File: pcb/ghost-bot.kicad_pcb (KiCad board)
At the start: 2 copper layers, 111 x 60 mm, 35 parts, among them J1 Conn_01x03_Pin, J2 Conn_01x03_Pin, J3 Conn_01x04_Pin, J4 Conn_01x02_Pin, SW1 SW_Push, SW2 SW_Push, SW3 Switch

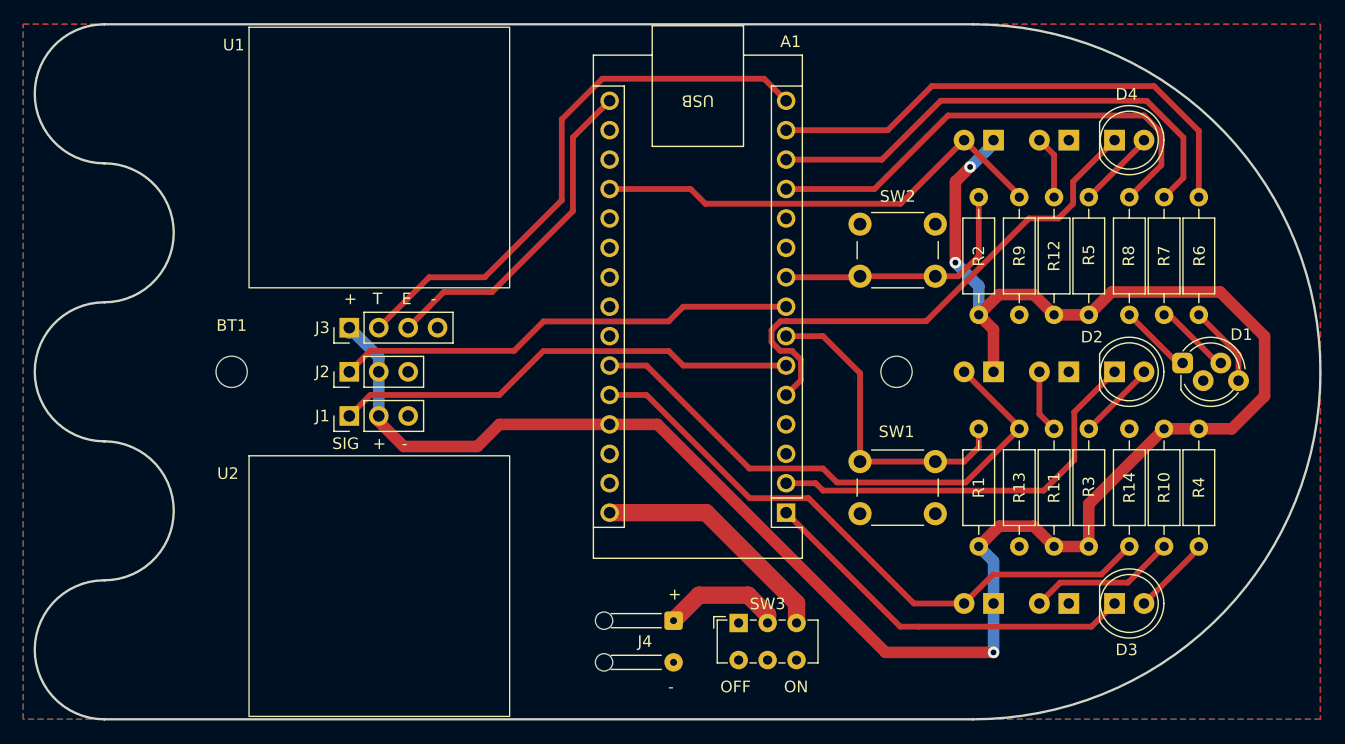
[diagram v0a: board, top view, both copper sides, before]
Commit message: Issue-6: Move LEDs, breakout unused pins
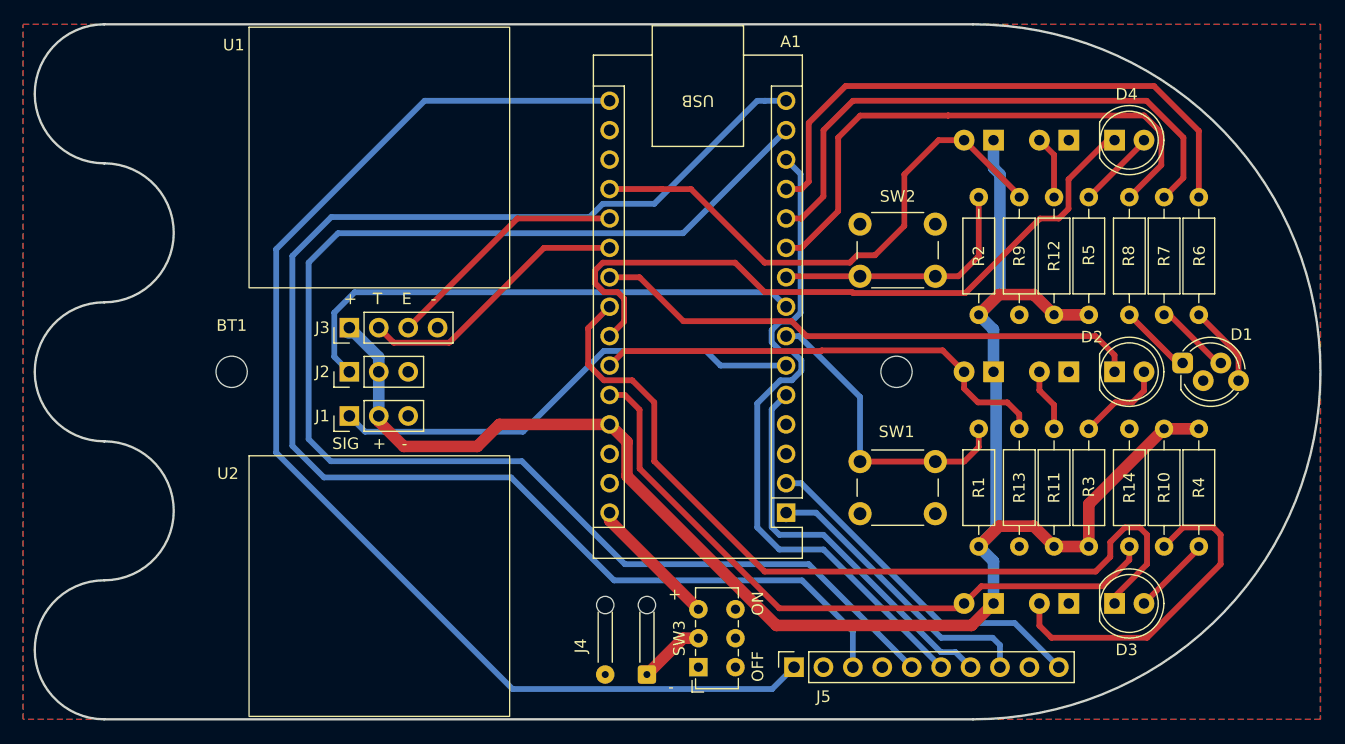
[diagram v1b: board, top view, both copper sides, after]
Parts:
- added J5: Conn_01x10, Connector_PinSocket_2.54mm:PinSocket_1x10_P2.54mm_Vertical, F.Cu at (167.1, 139.5)
- moved J4 5.19 mm to (154.4, 140.1), turned to 180 degrees
- moved SW3 5.16 mm to (158.8, 139.5), turned to 90 degrees
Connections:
- A1 pad 1: /LED1 -> /UART_TX
- A1 pad 10: unconnected-(A1-D7-Pad10) -> /RGB_B
- A1 pad 11: unconnected-(A1-D8-Pad11) -> /RGB_G
- A1 pad 12: /RGB_B -> /RGB_R
- A1 pad 13: /RGB_G -> /SPI_CC
- A1 pad 14: /RGB_R -> /SPI_MOSI
- A1 pad 15: /TRIG -> /SPI_MISO
- A1 pad 16: /ECHO -> /SPI_CLK
- A1 pad 2: /LED0 -> /UART_RX
- A1 pad 20: unconnected-(A1-A1-Pad20) -> /ECHO
- A1 pad 21: unconnected-(A1-A2-Pad21) -> /TRIG
- A1 pad 22: unconnected-(A1-A3-Pad22) -> /LED0
- A1 pad 23: unconnected-(A1-A4-Pad23) -> /LED1
- A1 pad 24: unconnected-(A1-A5-Pad24) -> /LED2
- A1 pad 5: /LED2 -> /GPIO_D2
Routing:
- net /SPI_MISO: track 0.00 -> 122.7 mm
- net /SPI_MOSI: track 0.00 -> 121.4 mm
- net /SPI_CLK: track 0.00 -> 105.6 mm
- net /SPI_CC: track 0.00 -> 58.6 mm
- net /LED1: track 33.3 -> 74.4 mm
- net /GPIO_D2: track 0.00 -> 34.5 mm
- net /UART_RX: track 0.00 -> 30.1 mm
- net /UART_TX: track 0.00 -> 25.7 mm
- net /TRIG: track 49.0 -> 23.9 mm
- net +5V: track 171.7 -> 154.3 mm, vias 3 -> 0
- net Net-(D6-A): track 12.8 -> 29.0 mm
- net /LED2: track 45.3 -> 61.1 mm
- net /LED0: track 35.3 -> 47.8 mm
- net +BATT_SW: track 21.1 -> 11.5 mm
- net /ECHO: track 29.2 -> 21.3 mm
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
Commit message: Separate UART and SPI connectors, reroute tracks, move buttons
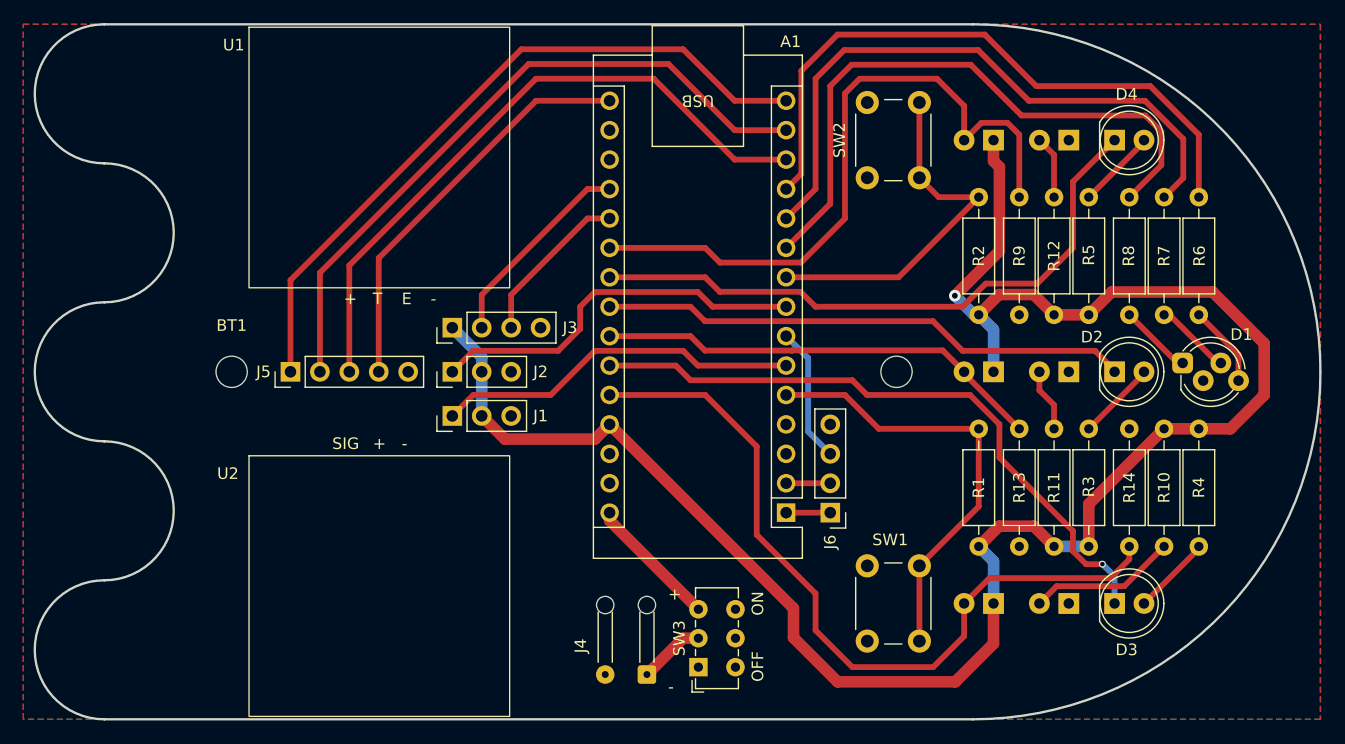
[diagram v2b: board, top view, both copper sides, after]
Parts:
- added J6: Conn_01x04_Pin, Connector_PinHeader_2.54mm:PinHeader_1x04_P2.54mm_Vertical, F.Cu at (170.2, 126.2)
- J5: value Conn_01x10 -> Conn_01x05_Pin; footprint Connector_PinSocket_2.54mm:PinSocket_1x10_P2.54mm_Vertical -> Connector_PinHeader_2.54mm:PinHeader_1x05_P2.54mm_Vertical
- moved J5 50.4 mm to (123.6, 114.0)
- moved SW1 12.5 mm to (173.4, 137.2), turned to 90 degrees
- moved J1 8.89 mm to (137.6, 117.8)
- moved J2 8.89 mm to (137.6, 114.0)
- moved J3 8.89 mm to (137.6, 110.2)
- moved SW2 4.05 mm to (173.4, 97.2), turned to 90 degrees
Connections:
- A1 pad 1: /UART_TX -> /UART_RX
- A1 pad 13: /SPI_CC -> /SPI_MISO
- A1 pad 15: /SPI_MISO -> /SPI_SS
- A1 pad 19: /PD0 -> /TRIG
- A1 pad 2: /UART_RX -> /UART_TX
- A1 pad 21: /TRIG -> /PD0
- A1 pad 22: /LED0 -> /LED2
- A1 pad 23: /LED1 -> /LED0
- A1 pad 24: /LED2 -> /PD1
- A1 pad 25: /PD1 -> /LED1
- A1 pad 5: /GPIO_D2 -> /PUSH_BTN0
- A1 pad 7: /PUSH_BTN0 -> /GPIO_D4
- J5 pad 1: /SPI_CLK -> /SPI_SS
- J5 pad 2: GND -> /SPI_MOSI
- J5 pad 4: GND -> /SPI_CLK
- J5 pad 5: /SPI_MOSI -> GND
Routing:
- net /SPI_CLK: track 105.6 -> 35.4 mm
- net /SPI_MISO: track 122.7 -> 56.5 mm
- net /SPI_MOSI: track 121.4 -> 58.6 mm
- net /SPI_SS: track 0.00 -> 60.8 mm
- net /SPI_CC: track 58.6 -> 0.00 mm
- net /GPIO_D2: track 34.5 -> 0.00 mm
- net /UART_RX: track 30.1 -> 3.81 mm
- net /UART_TX: track 25.7 -> 3.81 mm
- net /LED1: track 74.4 -> 56.2 mm, vias 0 -> 1
- net Net-(D6-A): track 29.0 -> 12.8 mm
- net /SERVO1: track 45.9 -> 33.3 mm
- net /PUSH_BTN0: track 26.5 -> 38.3 mm
- net /GPIO_D4: track 0.00 -> 11.7 mm
- net /PD0: track 47.5 -> 59.2 mm
- net +5V: track 154.3 -> 165.5 mm, vias 0 -> 1
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
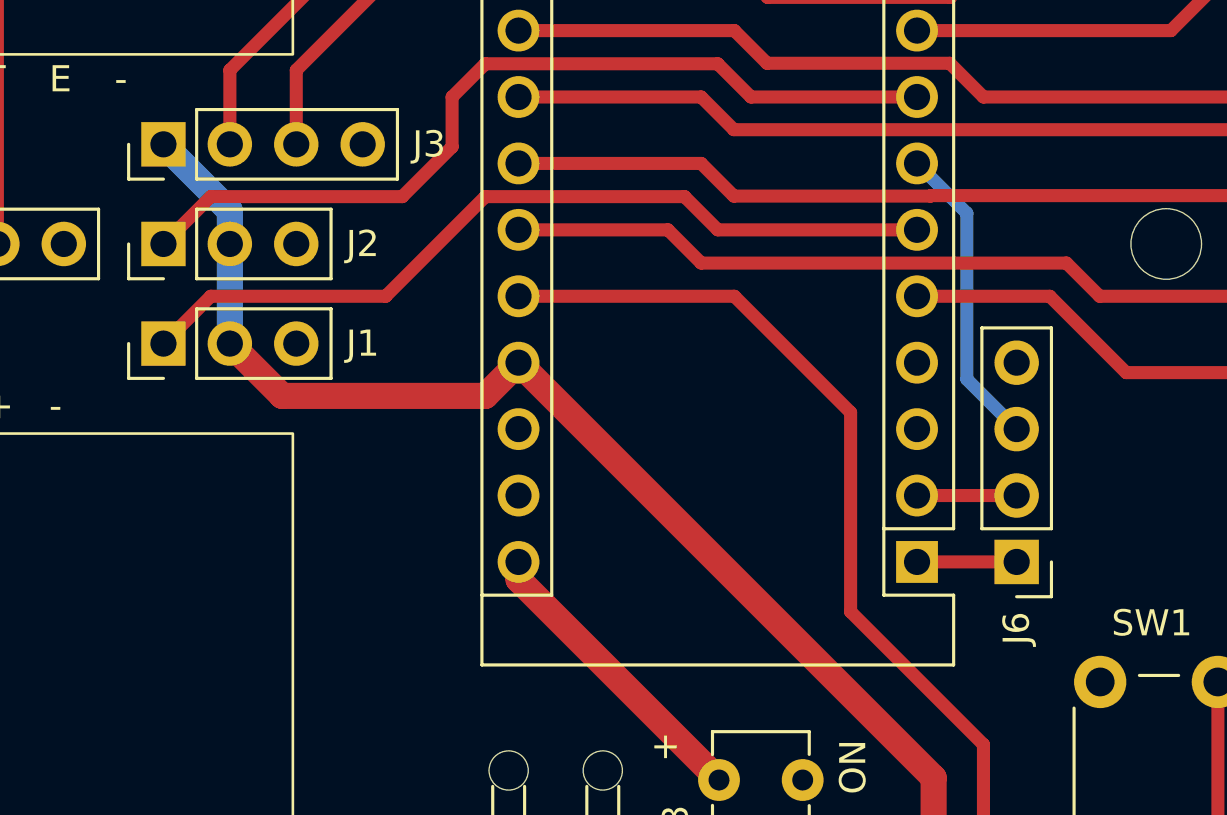
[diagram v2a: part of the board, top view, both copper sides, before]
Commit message: Resolve gnd thermal relief issues
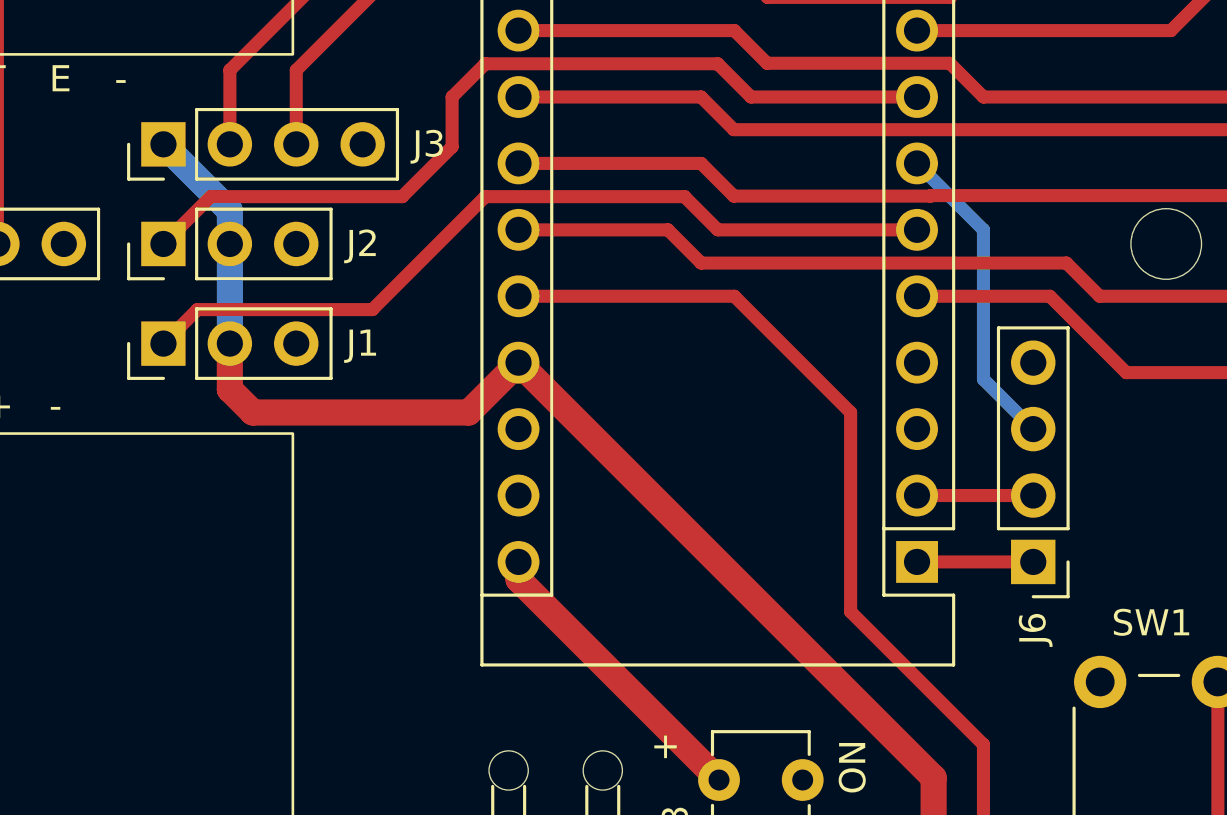
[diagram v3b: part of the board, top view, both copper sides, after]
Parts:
- moved J6 0.63 mm to (170.8, 126.2)
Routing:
- net +5V: track 165.5 -> 167.0 mm
- net /UART_TX: track 3.81 -> 4.44 mm
- net /UART_RX: track 3.81 -> 4.44 mm
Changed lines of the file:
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@@
 	(footprint "Connector_PinHeader_2.54mm:PinHeader_1x04_P2.54mm_Vertical"
 		(layer "F.Cu")
-		(at 170.18 126.16 180)
+		(at 170.815 126.16 180)
 		(descr "Through hole straight pin header, 1x04, 2.54mm pitch, single row")
 		(tags "Through hole pin header THT 1x04 2.54mm single row")
 		(property "Reference" "J6"
-			(at 0 -2.54 270)
+			(at 0 -2.54 -90)
 			(layer "F.SilkS")
 			(effects
@@
 		)
 		(fp_text user "${REFERENCE}"
-			(at 0 3.81 270)
+			(at 0 3.81 -90)
 			(layer "F.Fab")
 			(effects
@@
 		(tags "tact sw push 6mm")
 		(property "Reference" "SW1"
-			(at 8.745 1.98 360)
+			(at 8.745 1.98 0)
 			(layer "F.SilkS")
 			(effects
@@
 		)
 		(property "Value" "SW_Push"
-			(at 3.75 6.7 270)
+			(at 3.75 6.7 -90)
 			(layer "F.Fab")
 			(effects
@@
 		)
 		(fp_text user "${REFERENCE}"
-			(at 3.25 2.25 270)
+			(at 3.25 2.25 -90)
 			(layer "F.Fab")
 			(effects
@@
 		(tags "tact sw push 6mm")
 		(property "Reference" "SW2"
-			(at 3.25 -2.395 270)
+			(at 3.25 -2.395 -90)
 			(layer "F.SilkS")
 			(effects
@@
 		)
 		(property "Value" "SW_Push"
-			(at 3.75 6.7 270)
+			(at 3.75 6.7 -90)
 			(layer "F.Fab")
 			(effects
@@
 		)
 		(fp_text user "${REFERENCE}"
-			(at 3.25 4.75 270)
+			(at 3.25 4.75 -90)
 			(layer "F.Fab")
 			(effects
@@
 		)
 		(property "Value" "Conn_01x05_Pin"
-			(at 0 12.49 270)
+			(at 0 12.49 -90)
 			(layer "F.Fab")
 			(effects
@@
 		)
 		(fp_text user "${REFERENCE}"
-			(at 0 5.08 360)
+			(at 0 5.08 0)
 			(layer "F.Fab")
 			(effects
@@
 	)
 	(segment
-		(start 146.05 116)
-		(end 139.36 116)
+		(start 137.55 117.81)
+		(end 138.85 116.51)
 		(width 0.5)
 		(layer "F.Cu")
@@
 	)
 	(segment
-		(start 166.37 113.46)
+		(start 157.48 112.19)
 		(end 158.75 113.46)
 		(width 0.5)
@@
 	)
 	(segment
-		(start 139.36 116)
-		(end 137.55 117.81)
+		(start 138.85 116.51)
+		(end 145.54 116.51)
 		(width 0.5)
 		(layer "F.Cu")
@@
 	)
 	(segment
-		(start 157.48 112.19)
-		(end 149.86 112.19)
+		(start 158.75 113.46)
+		(end 166.37 113.46)
 		(width 0.5)
 		(layer "F.Cu")
@@
 	(segment
 		(start 149.86 112.19)
-		(end 146.05 116)
+		(end 157.48 112.19)
 		(width 0.5)
 		(layer "F.Cu")
@@
 	)
 	(segment
-		(start 158.75 113.46)
-		(end 157.48 112.19)
+		(start 145.54 116.51)
+		(end 149.86 112.19)
 		(width 0.5)
 		(layer "F.Cu")
@@
 	)
 	(segment
-		(start 140.09 117.81)
-		(end 142.09 119.81)
-		(width 1)
-		(layer "F.Cu")
-		(net 18)
-	)
-	(segment
 		(start 184.785 96.315)
 		(end 184.275003 95.805003)
@@
 	)
 	(segment
+		(start 140.97 120.445)
+		(end 149.225 120.445)
+		(width 1)
+		(layer "F.Cu")
+		(net 18)
+	)
+	(segment
+		(start 140.09 119.565)
+		(end 140.97 120.445)
+		(width 1)
+		(layer "F.Cu")
+		(net 18)
+	)
+	(segment
 		(start 189.500003 109.08)
 		(end 192.500003 109.08)
@@
 	)
 	(segment
+		(start 140.09 117.81)
+		(end 140.09 119.565)
+		(width 1)
+		(layer "F.Cu")
+		(net 18)
+	)
+	(segment
+		(start 149.225 120.445)
+		(end 151.13 118.54)
+		(width 1)
+		(layer "F.Cu")
+		(net 18)
+	)
+	(segment
 		(start 151.13 118.54)
 		(end 167.005 134.415)
@@
 	)
 	(segment
-		(start 142.09 119.81)
-		(end 149.86 119.81)
-		(width 1)
-		(layer "F.Cu")
-		(net 18)
-	)
-	(segment
-		(start 149.86 119.81)
-		(end 151.13 118.54)
-		(width 1)
-		(layer "F.Cu")
-		(net 18)
-	)
-	(segment
 		(start 204.725 118.92)
 		(end 207.645 116)
@@
 	(segment
 		(start 166.37 126.16)
-		(end 170.18 126.16)
+		(end 170.815 126.16)
 		(width 0.5)
 		(layer "F.Cu")
@@
 	(segment
 		(start 166.37 123.62)
-		(end 170.18 123.62)
+		(end 170.815 123.62)
 		(width 0.5)
 		(layer "F.Cu")
@@
 	)
 	(segment
-		(start 168.275 112.825)
+		(start 168.91 113.46)
 		(end 166.37 110.92)
 		(width 0.5)
@@
 	)
 	(segment
-		(start 168.275 119.175)
-		(end 168.275 112.825)
+		(start 170.815 121.08)
+		(end 168.91 119.175)
 		(width 0.5)
 		(layer "B.Cu")
@@
 	)
 	(segment
-		(start 170.18 121.08)
-		(end 168.275 119.175)
+		(start 168.91 119.175)
+		(end 168.91 113.46)
 		(width 0.5)
 		(layer "B.Cu")

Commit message: Change LED pins (again)
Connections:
- A1 pad 10: /RGB_B -> /PUSH_BTN1
- A1 pad 11: /RGB_G -> /SPI_SS
- A1 pad 12: /RGB_R -> /RGB_G
- A1 pad 13: /SPI_MISO -> /RGB_R
- A1 pad 15: /SPI_SS -> /SPI_MISO
- A1 pad 9: /PUSH_BTN1 -> /RGB_B
- J5 pad 1: /SPI_SS -> /SPI_MISO
- J5 pad 2: /SPI_MOSI -> GND
- J5 pad 3: /SPI_MISO -> /SPI_MOSI
- J5 pad 4: /SPI_CLK -> /SPI_SS
- J5 pad 5: GND -> /SPI_CLK
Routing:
- net /RGB_B: track 54.1 -> 36.9 mm
- net /PUSH_BTN1: track 31.8 -> 26.3 mm
- net /SPI_MISO: track 56.5 -> 60.8 mm
- net /SPI_SS: track 60.8 -> 57.5 mm
- net /RGB_G: track 54.8 -> 52.2 mm
- net /PD0: track 59.2 -> 56.6 mm
- net /RGB_R: track 55.3 -> 52.8 mm
- net /SPI_CLK: track 35.4 -> 34.3 mm
- net /SPI_MOSI: track 58.6 -> 57.6 mm
- net GND: vias 0 -> 1

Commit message: Update silkscreen
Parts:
- added G***: LOGO, LOGO, B.Cu at (131.0, 132.5)
- added G***: LOGO, LOGO, B.Cu at (131.0, 98.0)
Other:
- board text added: "CLK"
- board text added: "GHOST-BOT V1.0.0 0524"
- board text added: "GND"
- board text added: "MISO"
- board text added: "MOSI"
- board text added: "SS"
- board text removed: "GHOST-BOT V0.1.0 0424"
